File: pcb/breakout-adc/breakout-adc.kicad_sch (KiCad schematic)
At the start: 23 parts, among them J1 Screw_Terminal_01x04, J10 Conn_01x01_Pin, J11 X Data, J12 Y Data, J13 Conn_01x01_Pin, J14 Conn_01x01_Pin, J15 FX18-120P-0.8SV20, J2 Screw_Terminal_01x02, J3 Conn_01x01_Pin, J4 Conn_01x01_Pin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

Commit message: [adc][pcb] assigned footprints and dropped on pcb
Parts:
- C40, C41, C42: footprint (none) -> Capacitor_SMD:C_0402_1005Metric
- J1: footprint (none) -> Connector_Phoenix_MC:PhoenixContact_MC_1,5_4-G-3.81_1x04_P3.81mm_Horizontal
- J10, J13, J14, J3, J4, J5, J6, J7, J8, J9: footprint (none) -> TestPoint:TestPoint_Keystone_5000-5004_Miniature
- J11: value X Data -> Conn_01x12_Pin; footprint (none) -> Connector_PinHeader_2.54mm:PinHeader_1x12_P2.54mm_Vertical
- J12: value Y Data -> Conn_01x12_Pin; footprint (none) -> Connector_PinHeader_2.54mm:PinHeader_1x12_P2.54mm_Vertical
- J2: footprint (none) -> Connector_Phoenix_MC:PhoenixContact_MC_1,5_6-G-3.81_1x06_P3.81mm_Horizontal
- R1, R2, R3: footprint Resistor_SMD:R_0603_1608Metric -> Resistor_SMD:R_0805_2012Metric
- U8, U9: footprint SOT-363_DIO -> digikey-footprints:SOT-363
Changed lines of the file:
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@@
 			)
 		)
-		(property "Footprint" ""
+		(property "Footprint" "TestPoint:TestPoint_Keystone_5000-5004_Miniature"
 			(at 392.43 63.5 0)
 			(effects
@@
 			)
 		)
-		(property "Footprint" ""
+		(property "Footprint" "TestPoint:TestPoint_Keystone_5000-5004_Miniature"
 			(at 298.45 92.71 0)
 			(effects
@@
 			)
 		)
-		(property "Footprint" ""
+		(property "Footprint" "TestPoint:TestPoint_Keystone_5000-5004_Miniature"
 			(at 298.45 58.42 0)
 			(effects
@@
 			)
 		)
-		(property "Footprint" ""
+		(property "Footprint" "TestPoint:TestPoint_Keystone_5000-5004_Miniature"
 			(at 298.45 55.88 0)
 			(effects
@@
 			)
 		)
-		(property "Footprint" ""
+		(property "Footprint" "TestPoint:TestPoint_Keystone_5000-5004_Miniature"
 			(at 298.45 96.52 0)
 			(effects
@@
 			)
 		)
-		(property "Footprint" ""
+		(property "Footprint" "Capacitor_SMD:C_0402_1005Metric"
 			(at 181.61 144.78 0)
 			(effects
@@
 			)
 		)
-		(property "Value" "X Data"
+		(property "Value" "Conn_01x12_Pin"
 			(at 336.296 52.07 0)
 			(effects
@@
 			)
 		)
-		(property "Footprint" ""
+		(property "Footprint" "Connector_PinHeader_2.54mm:PinHeader_1x12_P2.54mm_Vertical"
 			(at 336.55 68.58 0)
 			(effects
@@
 			)
 		)
-		(property "Footprint" "Resistor_SMD:R_0603_1608Metric"
+		(property "Footprint" "Resistor_SMD:R_0805_2012Metric"
 			(at 76.2 93.98 0)
 			(effects
@@
 			)
 		)
-		(property "Footprint" "Resistor_SMD:R_0603_1608Metric"
+		(property "Footprint" "Resistor_SMD:R_0805_2012Metric"
 			(at 76.2 99.06 0)
 			(effects
@@
 			)
 		)
-		(property "Footprint" "SOT-363_DIO"
+		(property "Footprint" "digikey-footprints:SOT-363"
 			(at 111.76 49.53 0)
 			(effects
@@
 			)
 		)
-		(property "Datasheet" "D1213A-04S-7"
+		(property "Datasheet" "https://www.diodes.com/assets/Datasheets/D1213A-04S.pdf"
 			(at 111.76 49.53 0)
 			(effects
@@
 			)
 		)
-		(property "Value" "Y Data"
+		(property "Value" "Conn_01x12_Pin"
 			(at 368.046 52.07 0)
 			(effects
@@
 			)
 		)
-		(property "Footprint" ""
+		(property "Footprint" "Connector_PinHeader_2.54mm:PinHeader_1x12_P2.54mm_Vertical"
 			(at 368.3 68.58 0)
 			(effects
@@
 			)
 		)
-		(property "Footprint" ""
+		(property "Footprint" "Capacitor_SMD:C_0402_1005Metric"
 			(at 170.18 144.78 0)
 			(effects
@@
 			)
 		)
-		(property "Footprint" ""
+		(property "Footprint" "TestPoint:TestPoint_Keystone_5000-5004_Miniature"
 			(at 298.45 85.09 0)
 			(effects
@@
 			)
 		)
-		(property "Footprint" ""
+		(property "Footprint" "TestPoint:TestPoint_Keystone_5000-5004_Miniature"
 			(at 298.45 63.5 0)
 			(effects
@@
 			)
 		)
-		(property "Footprint" "SOT-363_DIO"
+		(property "Footprint" "digikey-footprints:SOT-363"
 			(at 111.76 97.79 0)
 			(effects
@@
 			)
 		)
-		(property "Datasheet" "D1213A-04S-7"
+		(property "Datasheet" "https://www.diodes.com/assets/Datasheets/D1213A-04S.pdf"
 			(at 111.76 97.79 0)
 			(effects
@@
 			)
 		)
-		(property "Footprint" ""
+		(property "Footprint" "Connector_Phoenix_MC:PhoenixContact_MC_1,5_4-G-3.81_1x04_P3.81mm_Horizontal"
 			(at 36.83 48.26 0)
 			(effects
@@
 			)
 		)
-		(property "Footprint" ""
+		(property "Footprint" "TestPoint:TestPoint_Keystone_5000-5004_Miniature"
 			(at 298.45 88.9 0)
 			(effects
@@
 			)
 		)
-		(property "Footprint" ""
+		(property "Footprint" "Connector_Phoenix_MC:PhoenixContact_MC_1,5_6-G-3.81_1x06_P3.81mm_Horizontal"
 			(at 36.83 90.17 0)
 			(effects
@@
 			)
 		)
-		(property "Footprint" ""
+		(property "Footprint" "Capacitor_SMD:C_0402_1005Metric"
 			(at 158.75 144.78 0)
 			(effects
@@
 			)
 		)
-		(property "Footprint" "Resistor_SMD:R_0603_1608Metric"
+		(property "Footprint" "Resistor_SMD:R_0805_2012Metric"
 			(at 76.2 96.52 0)
 			(effects
@@
 			)
 		)
-		(property "Footprint" ""
+		(property "Footprint" "TestPoint:TestPoint_Keystone_5000-5004_Miniature"
 			(at 392.43 60.96 0)
 			(effects
@@
 			)
 		)
-		(property "Footprint" ""
+		(property "Footprint" "TestPoint:TestPoint_Keystone_5000-5004_Miniature"
 			(at 298.45 60.96 0)
 			(effects

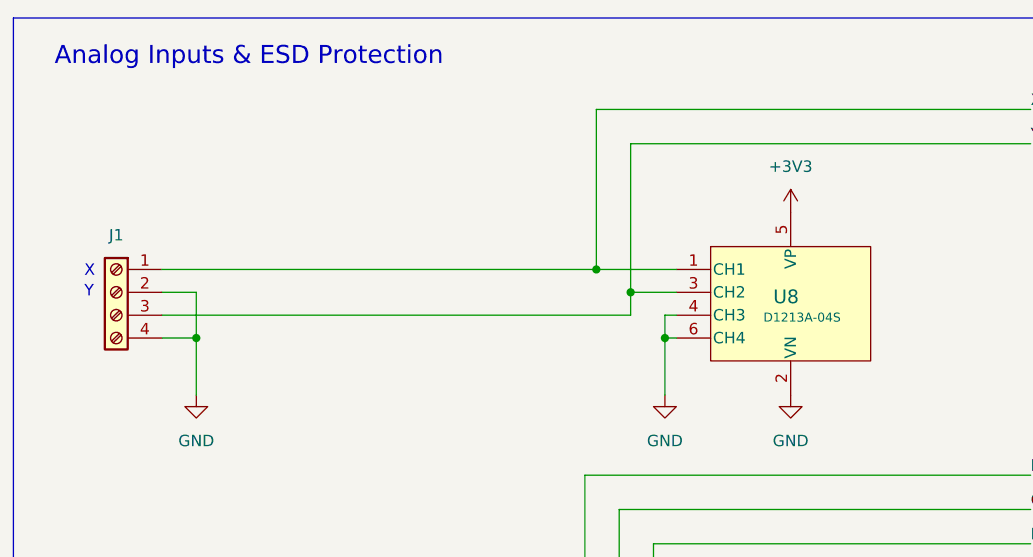
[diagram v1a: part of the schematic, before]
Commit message: [adc][pcb] initial layout of X input op amp
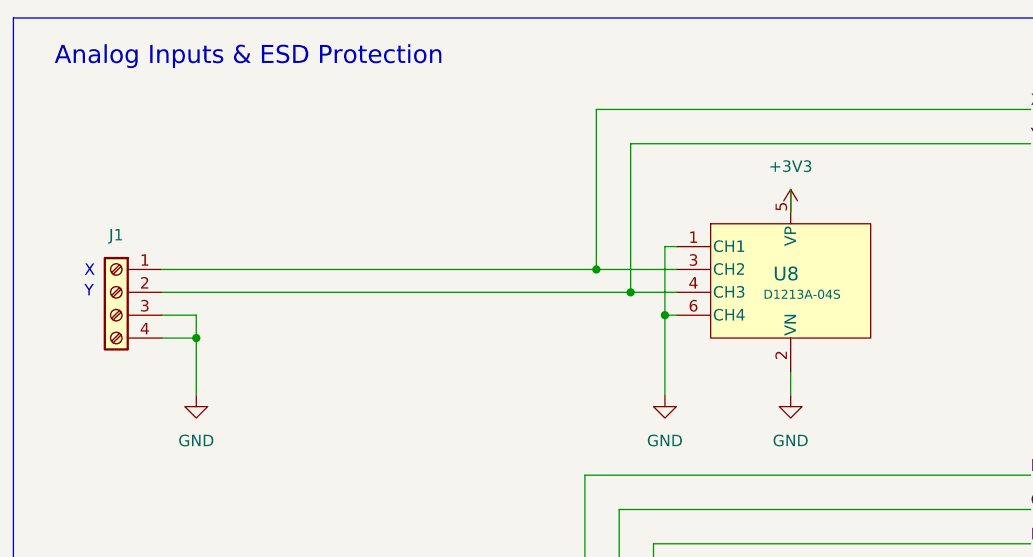
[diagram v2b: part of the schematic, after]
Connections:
- net GND: now also J1.3 (Pin_3), U8.1 (CH1); no longer J1.2 (Pin_2), U8.4 (CH3)
- net X: now also U8.3 (CH2); no longer U8.1 (CH1)
- net Y: now also J1.2 (Pin_2), U8.4 (CH3); no longer J1.3 (Pin_3), U8.3 (CH2)
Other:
- moved on the sheet: U8
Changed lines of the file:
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@@
 	)
 	(junction
-		(at 127 246.38)
+		(at 97.79 50.8)
 		(diameter 0)
 		(color 0 0 0 0)
 	)
 	(junction
-		(at 45.72 92.71)
+		(at 127 246.38)
 		(diameter 0)
 		(color 0 0 0 0)
 	)
 	(junction
-		(at 97.79 53.34)
+		(at 45.72 53.34)
 		(diameter 0)
 		(color 0 0 0 0)
 	)
 	(junction
-		(at 90.17 45.72)
+		(at 45.72 92.71)
 		(diameter 0)
 		(color 0 0 0 0)
@@
 	)
 	(junction
-		(at 45.72 53.34)
+		(at 90.17 45.72)
 		(diameter 0)
 		(color 0 0 0 0)
@@
 	(wire
 		(pts
-			(xy 129.54 205.74) (xy 123.19 205.74)
+			(xy 45.72 50.8) (xy 45.72 53.34)
 		)
 		(stroke
@@
 	(wire
 		(pts
-			(xy 92.71 96.52) (xy 92.71 72.39)
+			(xy 129.54 205.74) (xy 123.19 205.74)
 		)
 		(stroke
@@
 	(wire
 		(pts
-			(xy 41.91 53.34) (xy 45.72 53.34)
+			(xy 92.71 96.52) (xy 92.71 72.39)
 		)
 		(stroke
@@
 	(wire
 		(pts
-			(xy 93.98 48.26) (xy 99.06 48.26)
+			(xy 41.91 53.34) (xy 45.72 53.34)
 		)
 		(stroke
@@
 	(wire
 		(pts
+			(xy 111.76 36.83) (xy 111.76 39.37)
+		)
+		(stroke
+			(width 0)
+			(type default)
+		)
+	)
+	(wire
+		(pts
 			(xy 88.9 93.98) (xy 99.06 93.98)
 		)
@@
 	(wire
 		(pts
-			(xy 45.72 48.26) (xy 45.72 53.34)
+			(xy 93.98 48.26) (xy 99.06 48.26)
 		)
 		(stroke
@@
 	(wire
 		(pts
-			(xy 41.91 48.26) (xy 45.72 48.26)
+			(xy 41.91 48.26) (xy 93.98 48.26)
 		)
 		(stroke
@@
 	(wire
 		(pts
-			(xy 96.52 246.38) (xy 86.36 246.38)
+			(xy 41.91 50.8) (xy 45.72 50.8)
 		)
 		(stroke
@@
 	(wire
 		(pts
-			(xy 92.71 96.52) (xy 99.06 96.52)
+			(xy 96.52 246.38) (xy 86.36 246.38)
 		)
 		(stroke
@@
 	(wire
 		(pts
-			(xy 41.91 45.72) (xy 90.17 45.72)
+			(xy 92.71 96.52) (xy 99.06 96.52)
 		)
 		(stroke
@@
 	(wire
 		(pts
-			(xy 97.79 53.34) (xy 99.06 53.34)
+			(xy 97.79 50.8) (xy 99.06 50.8)
 		)
 		(stroke
@@
 	(wire
 		(pts
-			(xy 88.9 68.58) (xy 138.43 68.58)
+			(xy 99.06 43.18) (xy 97.79 43.18)
 		)
 		(stroke
@@
 	(wire
 		(pts
-			(xy 144.78 160.02) (xy 123.19 160.02)
+			(xy 88.9 68.58) (xy 138.43 68.58)
 		)
 		(stroke
@@
 	(wire
 		(pts
-			(xy 93.98 48.26) (xy 93.98 50.8)
+			(xy 144.78 160.02) (xy 123.19 160.02)
 		)
 		(stroke
@@
 	(wire
 		(pts
-			(xy 97.79 53.34) (xy 97.79 59.69)
-		)
-		(stroke
-			(width 0)
-			(type default)
-		)
-	)
-	(wire
-		(pts
 			(xy 41.91 97.79) (xy 45.72 97.79)
 		)
@@
 	(wire
 		(pts
-			(xy 41.91 50.8) (xy 93.98 50.8)
+			(xy 123.19 190.5) (xy 146.05 190.5)
 		)
 		(stroke
@@
 	(wire
 		(pts
-			(xy 123.19 190.5) (xy 146.05 190.5)
+			(xy 127 243.84) (xy 127 246.38)
 		)
 		(stroke
@@
 	(wire
 		(pts
-			(xy 127 243.84) (xy 127 246.38)
+			(xy 97.79 50.8) (xy 97.79 59.69)
 		)
 		(stroke
@@
 	(wire
 		(pts
-			(xy 90.17 45.72) (xy 90.17 27.94)
+			(xy 90.17 27.94) (xy 90.17 45.72)
 		)
 		(stroke
@@
 	(wire
 		(pts
+			(xy 41.91 45.72) (xy 90.17 45.72)
+		)
+		(stroke
+			(width 0)
+			(type default)
+		)
+	)
+	(wire
+		(pts
 			(xy 229.87 69.85) (xy 248.92 69.85)
 		)
@@
 	(wire
 		(pts
-			(xy 93.98 31.75) (xy 138.43 31.75)
+			(xy 111.76 57.15) (xy 111.76 59.69)
 		)
 		(stroke
@@
 	(wire
 		(pts
-			(xy 314.96 76.2) (xy 331.47 76.2)
+			(xy 93.98 31.75) (xy 138.43 31.75)
 		)
 		(stroke
@@
 	(wire
 		(pts
-			(xy 111.76 109.22) (xy 111.76 107.95)
+			(xy 314.96 76.2) (xy 331.47 76.2)
 		)
 		(stroke
@@
 	(wire
 		(pts
-			(xy 382.27 58.42) (xy 382.27 60.96)
+			(xy 111.76 109.22) (xy 111.76 107.95)
 		)
 		(stroke
@@
 	(wire
 		(pts
-			(xy 170.18 147.32) (xy 170.18 151.13)
+			(xy 382.27 58.42) (xy 382.27 60.96)
 		)
 		(stroke
@@
 	(wire
 		(pts
-			(xy 88.9 93.98) (xy 88.9 68.58)
+			(xy 170.18 147.32) (xy 170.18 151.13)
 		)
 		(stroke
@@
 	(wire
 		(pts
-			(xy 93.98 48.26) (xy 93.98 31.75)
+			(xy 88.9 93.98) (xy 88.9 68.58)
 		)
 		(stroke
@@
 	(wire
 		(pts
-			(xy 346.71 71.12) (xy 363.22 71.12)
+			(xy 97.79 43.18) (xy 97.79 50.8)
 		)
 		(stroke
@@
 	(wire
 		(pts
-			(xy 62.23 144.78) (xy 52.07 144.78)
+			(xy 346.71 71.12) (xy 363.22 71.12)
 		)
 		(stroke
@@
 	(wire
 		(pts
-			(xy 288.29 63.5) (xy 288.29 66.04)
+			(xy 62.23 144.78) (xy 52.07 144.78)
 		)
 		(stroke
@@
 	(wire
 		(pts
-			(xy 314.96 68.58) (xy 331.47 68.58)
+			(xy 288.29 63.5) (xy 288.29 66.04)
 		)
 		(stroke
@@
 	(wire
 		(pts
-			(xy 314.96 60.96) (xy 331.47 60.96)
+			(xy 314.96 68.58) (xy 331.47 68.58)
 		)
 		(stroke
@@
 	(wire
 		(pts
-			(xy 99.06 50.8) (xy 97.79 50.8)
+			(xy 314.96 60.96) (xy 331.47 60.96)
 		)
 		(stroke
@@
 	(wire
 		(pts
-			(xy 90.17 45.72) (xy 99.06 45.72)
-		)
-		(stroke
-			(width 0)
-			(type default)
-		)
-	)
-	(wire
-		(pts
 			(xy 123.19 198.12) (xy 146.05 198.12)
 		)
@@
 	(wire
 		(pts
+			(xy 90.17 45.72) (xy 99.06 45.72)
+		)
+		(stroke
+			(width 0)
+			(type default)
+		)
+	)
+	(wire
+		(pts
 			(xy 127 246.38) (xy 133.35 246.38)
 		)
@@
 	(wire
 		(pts
-			(xy 45.72 92.71) (xy 45.72 97.79)
+			(xy 93.98 31.75) (xy 93.98 48.26)
 		)
 		(stroke
@@
 	(wire
 		(pts
-			(xy 229.87 72.39) (xy 248.92 72.39)
+			(xy 45.72 92.71) (xy 45.72 97.79)
 		)
 		(stroke
@@
 	(wire
 		(pts
-			(xy 293.37 58.42) (xy 288.29 58.42)
+			(xy 229.87 72.39) (xy 248.92 72.39)
 		)
 		(stroke
@@
 	(wire
 		(pts
-			(xy 127 241.3) (xy 123.19 241.3)
+			(xy 293.37 58.42) (xy 288.29 58.42)
 		)
 		(stroke
@@
 	(wire
 		(pts
-			(xy 181.61 147.32) (xy 181.61 151.13)
+			(xy 127 241.3) (xy 123.19 241.3)
 		)
 		(stroke
@@
 	(wire
 		(pts
-			(xy 133.35 142.24) (xy 123.19 142.24)
+			(xy 181.61 147.32) (xy 181.61 151.13)
 		)
 		(stroke
@@
 	(wire
 		(pts
-			(xy 96.52 182.88) (xy 86.36 182.88)
+			(xy 133.35 142.24) (xy 123.19 142.24)
 		)
 		(stroke
@@
 	(wire
 		(pts
-			(xy 97.79 50.8) (xy 97.79 53.34)
+			(xy 96.52 182.88) (xy 86.36 182.88)
 		)
 		(stroke
@@
 		(lib_name "D1213A-04S-7_1")
 		(lib_id "D1213A-04S:D1213A-04S-7")
-		(at 111.76 49.53 0)
+		(at 111.76 46.99 0)
 		(unit 1)
 		(exclude_from_sim yes)
@@
 		(dnp no)
 		(property "Reference" "U8"
-			(at 111.252 48.768 0)
+			(at 111.252 46.228 0)
 			(effects
 				(font
@@
 		)
 		(property "Value" "D1213A-04S"
-			(at 113.03 51.054 0)
+			(at 113.03 48.514 0)
 			(effects
 				(font
@@
 		)
 		(property "Footprint" "digikey-footprints:SOT-363"
-			(at 111.76 49.53 0)
+			(at 111.76 46.99 0)
 			(effects
 				(font
@@
 		)
 		(property "Datasheet" "https://www.diodes.com/assets/Datasheets/D1213A-04S.pdf"
-			(at 111.76 49.53 0)
+			(at 111.76 46.99 0)
 			(effects
 				(font
@@
 		)
 		(property "Description" ""
-			(at 111.76 49.53 0)
+			(at 111.76 46.99 0)
 			(effects
 				(font

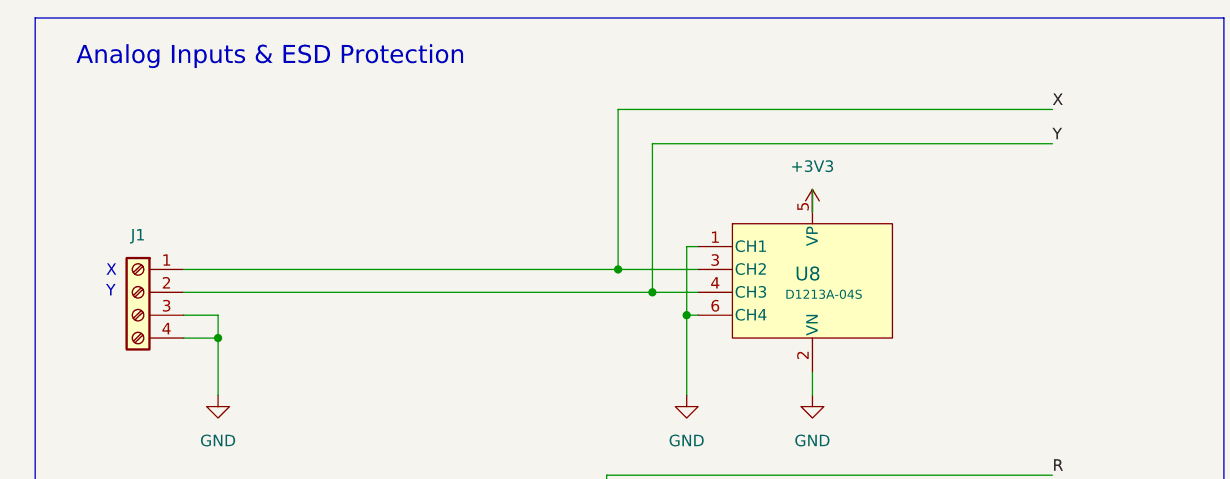
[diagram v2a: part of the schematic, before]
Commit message: [adc][pcb] initial start of place and route for ADC
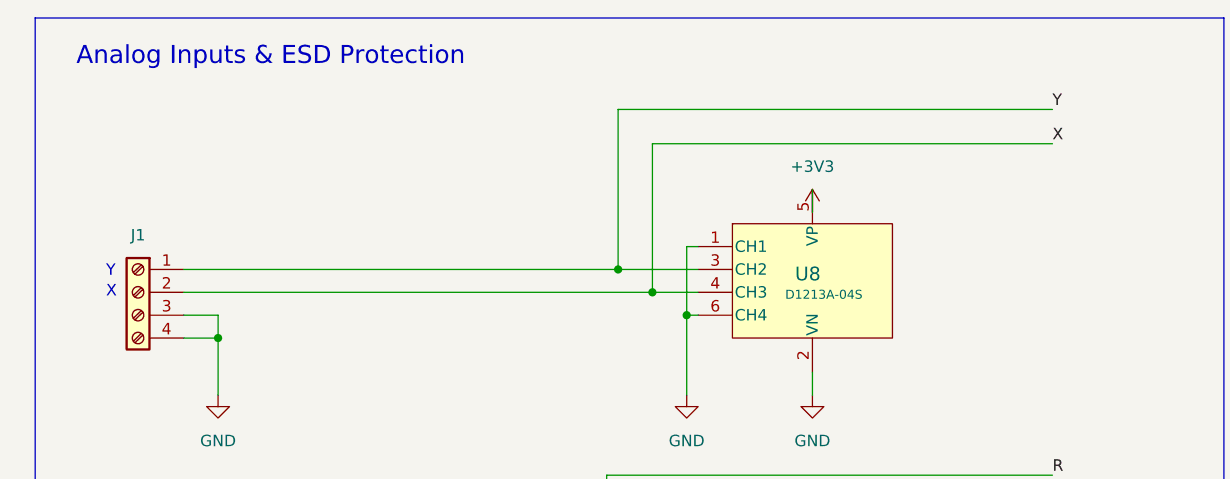
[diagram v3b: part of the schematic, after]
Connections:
- net X: now also J1.2 (Pin_2), U8.4 (CH3); no longer J1.1 (Pin_1), U8.3 (CH2)
- net Y: now also J1.1 (Pin_1), U8.3 (CH2); no longer J1.2 (Pin_2), U8.4 (CH3)
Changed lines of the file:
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@@
 	(text "Y"
 		(exclude_from_sim no)
-		(at 33.274 48.26 0)
+		(at 33.274 45.974 0)
 		(effects
 			(font
@@
 	(text "X"
 		(exclude_from_sim no)
-		(at 33.274 45.974 0)
+		(at 33.274 48.26 0)
 		(effects
 			(font
@@
 	)
 	(label "X"
-		(at 138.43 27.94 0)
+		(at 138.43 31.75 0)
 		(fields_autoplaced yes)
 		(effects
@@
 	)
 	(label "Y"
-		(at 138.43 31.75 0)
-		(fields_autoplaced yes)
-		(effects
+		(at 138.43 27.94 0)
+		(fields_autoplaced yes)
+		(effects

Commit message: [adc][pcb] redo of upper op amp
This also includes additional p&r of all components.
They are all in the pcb boundary now. This rev also
gives up on being fully single sided. See the layout.md
notes.

Lower op amp needs still needs to be placed and routed
like the upper one.
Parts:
- J11, J12: footprint Connector_PinHeader_2.54mm:PinHeader_1x12_P2.54mm_Vertical -> Connector_PinHeader_2.54mm:PinHeader_2x06_P2.54mm_Vertical
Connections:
- net +3V3: no longer U8.5 (VP)
- net GND: now also J1.1 (Pin_1); no longer J1.3 (Pin_3)
- net X: now also J1.3 (Pin_3); no longer J1.2 (Pin_2)
- net Y: now also J1.2 (Pin_2); no longer J1.1 (Pin_1)
- new net +3V3A: U8.5 (VP)
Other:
- moved on the sheet: J1
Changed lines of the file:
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@@
 	)
 	(junction
-		(at 45.72 53.34)
+		(at 93.98 48.26)
 		(diameter 0)
 		(color 0 0 0 0)
@@
 	)
 	(junction
-		(at 90.17 45.72)
-		(diameter 0)
-		(color 0 0 0 0)
-	)
-	(junction
 		(at 45.72 97.79)
 		(diameter 0)
@@
 	)
 	(junction
-		(at 93.98 48.26)
+		(at 88.9 93.98)
 		(diameter 0)
 		(color 0 0 0 0)
 	)
 	(junction
-		(at 88.9 93.98)
+		(at 127 236.22)
 		(diameter 0)
 		(color 0 0 0 0)
 	)
 	(junction
-		(at 127 236.22)
+		(at 90.17 45.72)
 		(diameter 0)
 		(color 0 0 0 0)
@@
 		(color 0 0 0 0)
 	)
+	(junction
+		(at 45.72 50.8)
+		(diameter 0)
+		(color 0 0 0 0)
+	)
 	(no_connect
 		(at 52.07 177.8)
@@
 	(wire
 		(pts
-			(xy 45.72 50.8) (xy 45.72 53.34)
-		)
-		(stroke
-			(width 0)
-			(type default)
-		)
-	)
-	(wire
-		(pts
 			(xy 129.54 205.74) (xy 123.19 205.74)
 		)
@@
 	(wire
 		(pts
-			(xy 41.91 53.34) (xy 45.72 53.34)
+			(xy 41.91 50.8) (xy 45.72 50.8)
 		)
 		(stroke
@@
 	(wire
 		(pts
-			(xy 45.72 53.34) (xy 45.72 59.69)
+			(xy 45.72 50.8) (xy 45.72 57.15)
 		)
 		(stroke
@@
 	(wire
 		(pts
-			(xy 41.91 48.26) (xy 93.98 48.26)
-		)
-		(stroke
-			(width 0)
-			(type default)
-		)
-	)
-	(wire
-		(pts
 			(xy 45.72 87.63) (xy 45.72 92.71)
 		)
@@
 	(wire
 		(pts
-			(xy 127 241.3) (xy 127 243.84)
+			(xy 41.91 48.26) (xy 93.98 48.26)
 		)
 		(stroke
@@
 	(wire
 		(pts
-			(xy 41.91 50.8) (xy 45.72 50.8)
+			(xy 127 241.3) (xy 127 243.84)
 		)
 		(stroke
@@
 	(wire
 		(pts
-			(xy 41.91 45.72) (xy 90.17 45.72)
-		)
-		(stroke
-			(width 0)
-			(type default)
-		)
-	)
-	(wire
-		(pts
 			(xy 229.87 69.85) (xy 248.92 69.85)
 		)
@@
 	(wire
 		(pts
+			(xy 41.91 45.72) (xy 90.17 45.72)
+		)
+		(stroke
+			(width 0)
+			(type default)
+		)
+	)
+	(wire
+		(pts
 			(xy 123.19 226.06) (xy 146.05 226.06)
 		)
@@
 	(wire
 		(pts
+			(xy 45.72 43.18) (xy 45.72 50.8)
+		)
+		(stroke
+			(width 0)
+			(type default)
+		)
+	)
+	(wire
+		(pts
 			(xy 293.37 60.96) (xy 288.29 60.96)
 		)
@@
 	(wire
 		(pts
+			(xy 41.91 43.18) (xy 45.72 43.18)
+		)
+		(stroke
+			(width 0)
+			(type default)
+		)
+	)
+	(wire
+		(pts
 			(xy 346.71 58.42) (xy 363.22 58.42)
 		)
@@
 		)
 	)
+	(text_box "Quesitons:\n\nBecause of it's position on the board, U8 (the ESD protection for X/Y) was referenced to the analog supply. I assume the internal diodes are quite and won't be a source of noise. Is this correct?"
+		(exclude_from_sim no)
+		(at 311.15 130.81 0)
+		(size 97.79 101.6)
+		(stroke
+			(width 0)
+			(type default)
+		)
+		(fill
+			(type none)
+		)
+		(effects
+			(font
+				(size 1.27 1.27)
+			)
+			(justify left top)
+		)
+	)
 	(text "Power Pins"
 		(exclude_from_sim no)
@@
 	(text "X"
 		(exclude_from_sim no)
-		(at 33.274 48.26 0)
+		(at 33.274 48.514 0)
 		(effects
 			(font
@@
 	(symbol
 		(lib_id "power:GND")
-		(at 45.72 59.69 0)
+		(at 45.72 57.15 0)
 		(unit 1)
 		(exclude_from_sim no)
@@
 		(fields_autoplaced yes)
 		(property "Reference" "#PWR0107"
-			(at 45.72 66.04 0)
+			(at 45.72 63.5 0)
 			(effects
 				(font
@@
 		)
 		(property "Value" "GND"
-			(at 45.72 64.77 0)
+			(at 45.72 62.23 0)
 			(effects
 				(font
@@
 		)
 		(property "Footprint" ""
-			(at 45.72 59.69 0)
+			(at 45.72 57.15 0)
 			(effects
 				(font
@@
 		)
 		(property "Datasheet" ""
-			(at 45.72 59.69 0)
+			(at 45.72 57.15 0)
 			(effects
 				(font
@@
 		)
 		(property "Description" "Power symbol creates a global label with name \"GND\" , ground"
-			(at 45.72 59.69 0)
+			(at 45.72 57.15 0)
 			(effects
 				(font
@@
 			)
 		)
-		(property "Footprint" "Connector_PinHeader_2.54mm:PinHeader_1x12_P2.54mm_Vertical"
+		(property "Footprint" "Connector_PinHeader_2.54mm:PinHeader_2x06_P2.54mm_Vertical"
 			(at 336.55 68.58 0)
 			(effects
@@
 			)
 		)
-		(property "Footprint" "Connector_PinHeader_2.54mm:PinHeader_1x12_P2.54mm_Vertical"
+		(property "Footprint" "Connector_PinHeader_2.54mm:PinHeader_2x06_P2.54mm_Vertical"
 			(at 368.3 68.58 0)
 			(effects
@@
 	(symbol
 		(lib_id "Connector:Screw_Terminal_01x04")
-		(at 36.83 48.26 0)
+		(at 36.83 45.72 0)
 		(mirror y)
 		(unit 1)
@@
 		(dnp no)
 		(property "Reference" "J1"
-			(at 36.83 41.91 0)
+			(at 36.83 39.37 0)
 			(effects
 				(font
@@
 		)
 		(property "Value" "Screw_Terminal_01x04"
-			(at 36.83 57.15 0)
+			(at 36.83 54.61 0)
 			(effects
 				(font
@@
 		)
 		(property "Footprint" "Connector_Phoenix_MC:PhoenixContact_MC_1,5_4-G-3.81_1x04_P3.81mm_Horizontal"
-			(at 36.83 48.26 0)
+			(at 36.83 45.72 0)
 			(effects
 				(font
@@
 		)
 		(property "Datasheet" "~"
-			(at 36.83 48.26 0)
+			(at 36.83 45.72 0)
 			(effects
 				(font
@@
 		)
 		(property "Description" "Generic screw terminal, single row, 01x04, script generated (kicad-library-utils/schlib/autogen/connector/)"
-			(at 36.83 48.26 0)
+			(at 36.83 45.72 0)
 			(effects
 				(font
@@
 			)
 		)
-		(property "Value" "+3V3"
+		(property "Value" "+3V3A"
 			(at 111.76 34.29 0)
 			(effects
